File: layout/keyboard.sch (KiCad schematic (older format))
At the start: 113 parts, among them U1 ProMicro

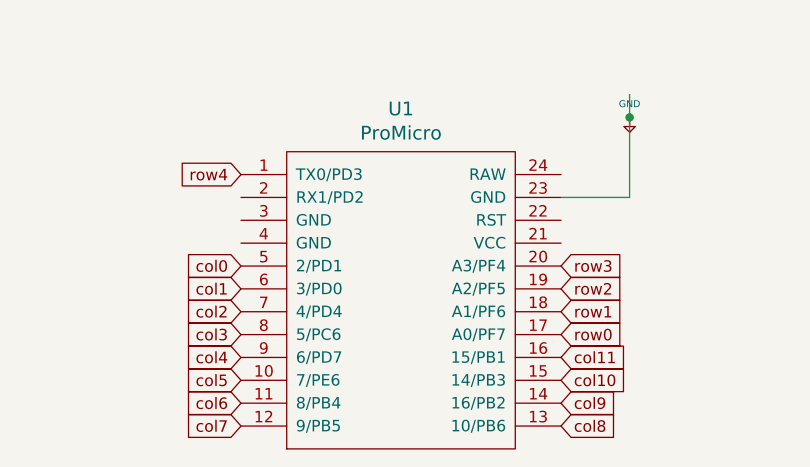
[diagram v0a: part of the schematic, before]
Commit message: routing to pro micro
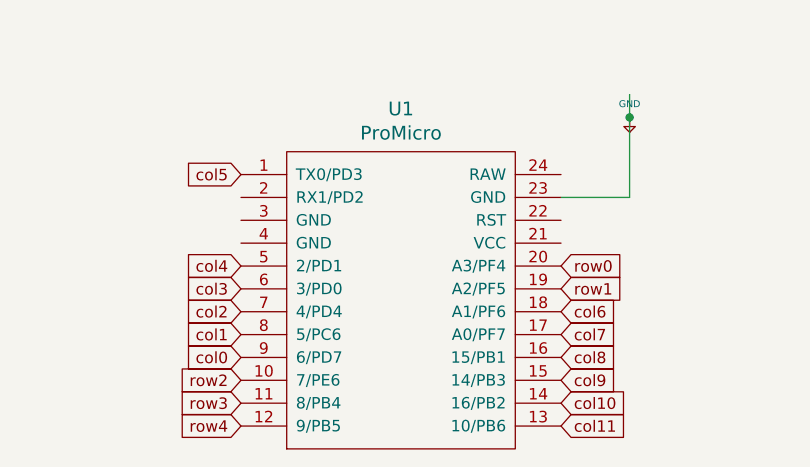
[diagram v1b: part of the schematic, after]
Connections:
- net col0: now also U1.9 (6/PD7); no longer U1.5 (2/PD1)
- net col1: now also U1.8 (5/PC6); no longer U1.6 (3/PD0)
- net col10: now also U1.14 (16/PB2); no longer U1.15 (14/PB3)
- net col11: now also U1.13 (10/PB6); no longer U1.16 (15/PB1)
- net col3: now also U1.6 (3/PD0); no longer U1.8 (5/PC6)
- net col4: now also U1.5 (2/PD1); no longer U1.9 (6/PD7)
- net col5: now also U1.1 (TX0/PD3); no longer U1.10 (7/PE6)
- net col6: now also U1.18 (A1/PF6); no longer U1.11 (8/PB4)
- net col7: now also U1.17 (A0/PF7); no longer U1.12 (9/PB5)
- net col8: now also U1.16 (15/PB1); no longer U1.13 (10/PB6)
- net col9: now also U1.15 (14/PB3); no longer U1.14 (16/PB2)
- net row0: now also U1.20 (A3/PF4); no longer U1.17 (A0/PF7)
- net row1: now also U1.19 (A2/PF5); no longer U1.18 (A1/PF6)
- net row2: now also U1.10 (7/PE6); no longer U1.19 (A2/PF5)
- net row3: now also U1.11 (8/PB4); no longer U1.20 (A3/PF4)
- net row4: now also U1.12 (9/PB5); no longer U1.1 (TX0/PD3)
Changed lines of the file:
@@
 $EndComp
 Text GLabel 6950 7900 0    50   Input ~ 0
-col0
+col4
 Text GLabel 6950 8000 0    50   Input ~ 0
-col1
+col3
 Text GLabel 6950 8100 0    50   Input ~ 0
 col2
 Text GLabel 6950 8200 0    50   Input ~ 0
-col3
+col1
 Text GLabel 6950 8300 0    50   Input ~ 0
-col4
+col0
 Text GLabel 6950 8400 0    50   Input ~ 0
-col5
+row2
 Text GLabel 6950 8500 0    50   Input ~ 0
+row3
+Text GLabel 6950 8600 0    50   Input ~ 0
+row4
+Text GLabel 8350 8600 2    50   Input ~ 0
+col11
+Text GLabel 8350 8500 2    50   Input ~ 0
+col10
+Text GLabel 8350 8400 2    50   Input ~ 0
+col9
+Text GLabel 8350 8300 2    50   Input ~ 0
+col8
+Text GLabel 8350 8200 2    50   Input ~ 0
+col7
+Text GLabel 8350 8100 2    50   Input ~ 0
 col6
-Text GLabel 6950 8600 0    50   Input ~ 0
-col7
-Text GLabel 8350 8600 2    50   Input ~ 0
-col8
-Text GLabel 8350 8500 2    50   Input ~ 0
-col9
-Text GLabel 8350 8400 2    50   Input ~ 0
-col10
-Text GLabel 8350 8300 2    50   Input ~ 0
-col11
-Text GLabel 8350 8200 2    50   Input ~ 0
+Text GLabel 8350 8000 2    50   Input ~ 0
+row1
+Text GLabel 8350 7900 2    50   Input ~ 0
 row0
-Text GLabel 8350 8100 2    50   Input ~ 0
-row1
-Text GLabel 8350 8000 2    50   Input ~ 0
-row2
-Text GLabel 8350 7900 2    50   Input ~ 0
-row3
 Wire Wire Line
 	8350 7600 8650 7600
@@
 	8650 7250 8650 7600
 Text GLabel 6950 7500 0    50   Input ~ 0
-row4
+col5
 $EndSCHEMATC

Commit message: fix gnd
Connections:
- net +5V is gone; now on net GND: U1.23 (GND)
- net GND: now reaches U1.3 (GND)
- net GND: now also U1.4 (GND)
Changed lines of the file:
@@
-	1    0    0    -1
-$EndComp
-$Comp
-L keyboard_parts:GND #PWR0101
-U 1 1 603330CF
-P 8650 7250
-F 0 "#PWR0101" H 8650 7300 20  0001 C CNN
-F 1 "GND" H 8650 7309 30  0000 C CNN
-F 2 "" H 8650 7250 60  0000 C CNN
-F 3 "" H 8650 7250 60  0000 C CNN
-	1    8650 7250
 	1    0    0    -1
 $EndComp
@@
 Text GLabel 8350 7900 2    50   Input ~ 0
 row0
-Wire Wire Line
-	8350 7600 8650 7600
-Wire Wire Line
-	8650 7150 8650 7250
-Connection ~ 8650 7250
-Wire Wire Line
-	8650 7250 8650 7600
 Text GLabel 6950 7500 0    50   Input ~ 0
 col5
+$Comp
+L power:GND #PWR?
+U 1 1 60410D36
+P 8850 7600
+F 0 "#PWR?" H 8850 7350 50  0001 C CNN
+F 1 "GND" H 8855 7427 50  0000 C CNN
+F 2 "" H 8850 7600 50  0001 C CNN
+F 3 "" H 8850 7600 50  0001 C CNN
+	1    8850 7600
+	1    0    0    -1
+$EndComp
+Wire Wire Line
+	8350 7600 8850 7600
+$Comp
+L power:GND #PWR?
+U 1 1 6049377B
+P 6600 7700
+F 0 "#PWR?" H 6600 7450 50  0001 C CNN
+F 1 "GND" H 6605 7527 50  0000 C CNN
+F 2 "" H 6600 7700 50  0001 C CNN
+F 3 "" H 6600 7700 50  0001 C CNN
+	1    6600 7700
+	1    0    0    -1
+$EndComp
+Wire Wire Line
+	6950 7700 6800 7700
+Wire Wire Line
+	6950 7800 6800 7800
+Wire Wire Line
+	6800 7800 6800 7700
+Connection ~ 6800 7700
+Wire Wire Line
+	6800 7700 6600 7700
 $EndSCHEMATC

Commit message: Updating with latest stuff
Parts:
- K_SPACE1, K_SPACE2: footprint MX_Only:MXOnly-2.25U-NoLED -> MX_Only:MXOnly-2.25U-ReversedStabilizers-NoLED
- U1: symbol keebio:ProMicro -> keyboard-rescue:ProMicro-keebio
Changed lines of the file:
@@
 F 0 "K_SPACE2" H 6500 5233 60  0000 C CNN
 F 1 "KEYSW" H 6500 4900 60  0001 C CNN
-F 2 "MX_Only:MXOnly-2.25U-NoLED" H 6500 5000 60  0001 C CNN
+F 2 "MX_Only:MXOnly-2.25U-ReversedStabilizers-NoLED" H 6500 5000 60  0001 C CNN
 F 3 "" H 6500 5000 60  0000 C CNN
 	1    6500 5000
@@
 F 0 "K_SPACE1" H 8500 5233 60  0000 C CNN
 F 1 "KEYSW" H 8500 4900 60  0001 C CNN
-F 2 "MX_Only:MXOnly-2.25U-NoLED" H 8500 5000 60  0001 C CNN
+F 2 "MX_Only:MXOnly-2.25U-ReversedStabilizers-NoLED" H 8500 5000 60  0001 C CNN
 F 3 "" H 8500 5000 60  0000 C CNN
 	1    8500 5000
@@
 	900  5400 2150 5400
 $Comp
-L keebio:ProMicro U1
+L keyboard-rescue:ProMicro-keebio U1
 U 1 1 602F1431
 P 7650 8050
@@
 col5
 $Comp
-L power:GND #PWR?
+L power:GND #PWR0101
 U 1 1 60410D36
 P 8850 7600
-F 0 "#PWR?" H 8850 7350 50  0001 C CNN
+F 0 "#PWR0101" H 8850 7350 50  0001 C CNN
 F 1 "GND" H 8855 7427 50  0000 C CNN
 F 2 "" H 8850 7600 50  0001 C CNN
@@
 	8350 7600 8850 7600
 $Comp
-L power:GND #PWR?
+L power:GND #PWR0102
 U 1 1 6049377B
 P 6600 7700
-F 0 "#PWR?" H 6600 7450 50  0001 C CNN
+F 0 "#PWR0102" H 6600 7450 50  0001 C CNN
 F 1 "GND" H 6605 7527 50  0000 C CNN
 F 2 "" H 6600 7700 50  0001 C CNN

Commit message: add 60% version
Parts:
- D_0, D_1, D_2, D_3, D_4, D_5, D_6, D_7, D_8, D_9, D_A1, D_ALT1, D_B1, D_BKSP1, D_BSLSH1, D_C1, D_CBRAC1, D_COMMA1, D_CTRL1, D_D1, D_DOT1, D_E1, D_EQUAL1, D_ESC1, D_F1, D_G1, D_H1, D_I1, D_J1, D_K1, D_L1, D_M1, D_MINUS1, D_N1, D_O1, D_OBRAC1, D_P1, D_Q1, D_QUOTE1, D_R1, D_S1, D_SEMIC1, D_SHIFT1, D_SLASH1, D_SPACE1, D_SPACE2, D_SUPER1, D_T1, D_TAB1, D_U1, D_V1, D_W1, D_X1, D_Y1, D_Z1, D_`1: footprint keyboard_parts:D_SOD123_axial -> Diode_SMD:D_SOD-123
- K_0, K_1, K_2, K_3, K_4, K_5, K_6, K_7, K_8, K_9, K_A1, K_B1, K_C1, K_CBRAC1, K_COMMA1, K_D1, K_DOT1, K_E1, K_EQUAL1, K_ESC1, K_F1, K_G1, K_H1, K_I1, K_J1, K_K1, K_L1, K_M1, K_MINUS1, K_N1, K_O1, K_OBRAC1, K_P1, K_Q1, K_QUOTE1, K_R1, K_S1, K_SEMIC1, K_SLASH1, K_T1, K_U1, K_V1, K_W1, K_X1, K_Y1, K_Z1, K_`1: footprint MX_Only:MXOnly-1U-NoLED -> MX_Only:MXOnly-1U-Hotswap
- K_ALT1, K_SUPER1: footprint MX_Only:MXOnly-1.25U-NoLED -> MX_Only:MXOnly-1.25U-Hotswap
- K_BKSP1: footprint MX_Only:MXOnly-2U-NoLED -> MX_Only:MXOnly-2U-Hotswap
- K_BSLSH1, K_TAB1: footprint MX_Only:MXOnly-1.5U-NoLED -> MX_Only:MXOnly-1.5U-Hotswap
- K_CTRL1: footprint MX_Only:MXOnly-1.75U-NoLED -> MX_Only:MXOnly-1U-Hotswap
- K_SHIFT1: footprint MX_Only:MXOnly-2.25U-NoLED -> MX_Only:MXOnly-2.25U-Hotswap
- K_SPACE1, K_SPACE2: footprint MX_Only:MXOnly-2.25U-ReversedStabilizers-NoLED -> MX_Only:MXOnly-2.25U-Hotswap-ReversedStabilizers
- U1: footprint Keebio-Parts:ArduinoProMicro -> Keebio-Parts:ArduinoProMicro-ZigZag
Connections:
- net col0: now also U1.19 (A2/PF5); no longer U1.9 (6/PD7)
- net col1: now also U1.18 (A1/PF6); no longer U1.8 (5/PC6)
- net col10: now also U1.7 (4/PD4); no longer U1.14 (16/PB2)
- net col11: now also U1.8 (5/PC6); no longer U1.13 (10/PB6)
- net col2: now also U1.17 (A0/PF7); no longer U1.7 (4/PD4)
- net col3: now also U1.16 (15/PB1); no longer U1.6 (3/PD0)
- net col4: now also U1.15 (14/PB3); no longer U1.5 (2/PD1)
- net col5: now also U1.14 (16/PB2); no longer U1.1 (TX0/PD3)
- net col6: now also U1.13 (10/PB6); no longer U1.18 (A1/PF6)
- net col7: now also U1.2 (RX1/PD2); no longer U1.17 (A0/PF7)
- net col8: now also U1.5 (2/PD1); no longer U1.16 (15/PB1)
- net col9: now also U1.6 (3/PD0); no longer U1.15 (14/PB3)
- net row1: now also U1.1 (TX0/PD3); no longer U1.19 (A2/PF5)
- net row2: now also U1.9 (6/PD7); no longer U1.10 (7/PE6)
- net row3: now also U1.10 (7/PE6); no longer U1.11 (8/PB4)
- net row4: now also U1.11 (8/PB4); no longer U1.12 (9/PB5)
